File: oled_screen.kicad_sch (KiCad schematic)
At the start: 7 parts, among them U38 0.96 OLED Display 8 pins

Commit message: SBCv0.3
there is no big thing update just some LCSC & Mouser parts
and Big problem deleted alot of component values (:
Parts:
- removed C397: 10u, Capacitor_SMD:C_0201_0603Metric_Pad0.64x0.40mm_HandSolder, symbol New_Library_0:C_Small_edited
- added C112: 10u, Capacitor_SMD:C_0603_1608Metric, symbol New_Library_0:C_Small_edited
- C394: LCSC Part (none) -> C19702; Mouser Part (none) -> 187-CL10A106KP8NNNC
- C395, C396: LCSC Part (none) -> C5209398; Mouser Part (none) -> CL03A105KP3NSNC
- R188: value 10k -> (none); LCSC Part (none) -> (at 0 0 0)
- R189: value 100R -> (none); LCSC Part (none) -> (polyline
- U38: value 0.96 OLED Display 8 pins -> (none); LCSC Part C5139767 -> (none); Mouser Part (none) -> )
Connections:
- net GND: now also C112.2
- net OLED_LED: now also C112.1

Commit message: SBCv0.4
add LCSC & Mouser parts 
and solve the deleted value in the past version
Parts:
- removed R188: (no value), PCM_Resistor_SMD_AKL:R_0402_1005Metric, symbol Device:R_Small
- removed U38: (no value), Datasheet_Footprints:FFC-SMD_8P-P0.50_AFC42-S08FMA-1H_BOTTOM, symbol Datasheet_Symbols:OLED Dosplay 8 pins
- added R246: 240R, PCM_Resistor_SMD_AKL:R_0402_1005Metric, symbol Device:R_Small
- added U53: 0.96 OLED Display 8 pins, Datasheet_Footprints:FFC-SMD_8P-P0.50_AFC42-S08FMA-1H_BOTTOM, symbol Datasheet_Symbols:OLED Dosplay 8 pins
- R189: value (none) -> 10k; footprint PCM_Resistor_SMD_AKL:R_0402_1005Metric_Pad0.72x0.64mm -> PCM_Resistor_SMD_AKL:R_0402_1005Metric; LCSC Part (polyline -> C60490; Mouser Part (none) -> 603-RC0402FR-0710KL
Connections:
- net GND: now also U53.2 (GND)
- net OLED_CLK: now also U53.6 (SCL)
- net OLED_CS: now also U53.8 (CS)
- net OLED_LED: now also R246.2, U53.1 (LEDA); no longer R189.2
- net OLED_MOSI: now also U53.5 (SDA)
- net OLED_RESET: now also R189.2, U53.3 (RESET)
- net OLED_RS: now also U53.4 (RS)
- net VCC5V0_SYS: now also R246.1; no longer R189.1
- net VCC_3V3_S0: now also R189.1, U53.7 (VDD)

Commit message: Release v2: replace main with RK3576 SBCv2, archive v1 to branch archive/v1
- main now shows only v2 (RK3576 SBCv2.kicad_pro)
- v1 preserved in branch archive/v1 + tag v1.0
- Add .gitignore for KiCad (*.bak, *.lck, .history/)
- Update README with version switcher
- Cleaned: dropped 141M .history, Resources ref PDF, *.bak/*.lck
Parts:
- removed R189: 10k, PCM_Resistor_SMD_AKL:R_0402_1005Metric, symbol Device:R_Small
- removed R246: 240R, PCM_Resistor_SMD_AKL:R_0402_1005Metric, symbol Device:R_Small
- added R197: 10k, PCM_Resistor_SMD_AKL:R_0402_1005Metric, symbol Device:R_Small
- added R251: 240R, PCM_Resistor_SMD_AKL:R_0402_1005Metric, symbol Device:R_Small
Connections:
- net OLED_LED: now also R251.2
- net OLED_RESET: now also R197.2
- net VCC5V0_SYS: now also R251.1
- net VCC_3V3_S0: now also R197.1

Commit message: Relink hierarchical root: 18 sheets into RK3576 SBCv2 top level
Root was empty (no sheet boxes); all subsheets orphaned.
Rebuilt A1 top level linking RK3576, LPDDR5, Power, Ethernet,
HDMI, MIPI, PCIe, USB-A/C, Wireless, RTC, uSD, GPIO, OLED,
RP2350A, Connectors, Fixtures, DC_Power. block_diagrame kept
docs-only (unlinked, avoids double-instantiation). Lowercase
stub duplicates excluded. ERC: 1388 -> 770 violations.
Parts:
- removed U53: 0.96 OLED Display 8 pins, Datasheet_Footprints:FFC-SMD_8P-P0.50_AFC42-S08FMA-1H_BOTTOM, symbol Datasheet_Symbols:OLED Dosplay 8 pins
- added U45: 0.96 OLED Display 8 pins, Datasheet_Footprints:FFC-SMD_8P-P0.50_AFC42-S08FMA-1H_BOTTOM, symbol Datasheet_Symbols:OLED Dosplay 8 pins
- renumbered C394 to C343, C395 to C344, C396 to C345, C112 to C346, R251 to R205, R197 to R206
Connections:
- net GND: now also U45.2 (GND)
- net OLED_CLK: now also U45.6 (SCL)
- net OLED_CS: now also U45.8 (CS)
- net OLED_LED: now also U45.1 (LEDA)
- net OLED_MOSI: now also U45.5 (SDA)
- net OLED_RESET: now also U45.3 (RESET)
- net OLED_RS: now also U45.4 (RS)
- net VCC_3V3_S0: now also U45.7 (VDD)
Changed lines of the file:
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@@
 		(in_pos_files yes)
 		(dnp no)
-		(property "Reference" "#PWR0573"
+		(property "Reference" "#PWR0520"
 			(at 96.52 92.71 0)
 			(hide yes)
@@
 			(project "RK3576 SBCv2"
 				(path "/802f5b9f-44c6-4b1a-a63a-2c094d5816db/07d8ed82-8848-42fe-9400-02853b4a0afe"
-					(reference "#PWR0573")
+					(reference "#PWR0520")
 					(unit 1)
 				)
@@
 		(in_pos_files yes)
 		(dnp no)
-		(property "Reference" "#PWR0570"
+		(property "Reference" "#PWR0517"
 			(at 53.34 80.01 0)
 			(hide yes)
@@
 			(project "RK3576 SBCv2"
 				(path "/802f5b9f-44c6-4b1a-a63a-2c094d5816db/07d8ed82-8848-42fe-9400-02853b4a0afe"
-					(reference "#PWR0570")
+					(reference "#PWR0517")
 					(unit 1)
 				)
@@
 		(dnp no)
 		(fields_autoplaced yes)
-		(property "Reference" "C394"
+		(property "Reference" "C343"
 			(at 55.88 49.5362 0)
 			(show_name no)
@@
 			(project "RK3576 SBCv2"
 				(path "/802f5b9f-44c6-4b1a-a63a-2c094d5816db/07d8ed82-8848-42fe-9400-02853b4a0afe"
-					(reference "C394")
+					(reference "C343")
 					(unit 1)
 				)
@@
 		(in_pos_files yes)
 		(dnp no)
-		(property "Reference" "#PWR0572"
+		(property "Reference" "#PWR0519"
 			(at 85.09 92.71 0)
 			(hide yes)
@@
 			(project "RK3576 SBCv2"
 				(path "/802f5b9f-44c6-4b1a-a63a-2c094d5816db/07d8ed82-8848-42fe-9400-02853b4a0afe"
-					(reference "#PWR0572")
+					(reference "#PWR0519")
 					(unit 1)
 				)
@@
 		(in_pos_files yes)
 		(dnp no)
-		(property "Reference" "#PWR0568"
+		(property "Reference" "#PWR0515"
 			(at 53.34 49.53 0)
 			(hide yes)
@@
 			(project "RK3576 SBCv2"
 				(path "/802f5b9f-44c6-4b1a-a63a-2c094d5816db/07d8ed82-8848-42fe-9400-02853b4a0afe"
-					(reference "#PWR0568")
+					(reference "#PWR0515")
 					(unit 1)
 				)
@@
 		(in_pos_files yes)
 		(dnp no)
-		(property "Reference" "R251"
+		(property "Reference" "R205"
 			(at 59.69 80.01 90)
 			(show_name no)
@@
 			(project "RK3576 SBCv2"
 				(path "/802f5b9f-44c6-4b1a-a63a-2c094d5816db/07d8ed82-8848-42fe-9400-02853b4a0afe"
-					(reference "R251")
+					(reference "R205")
 					(unit 1)
 				)
@@
 		(in_pos_files yes)
 		(dnp no)
-		(property "Reference" "R197"
+		(property "Reference" "R206"
 			(at 85.344 49.53 0)
 			(show_name no)
@@
 			(project "RK3576 SBCv2"
 				(path "/802f5b9f-44c6-4b1a-a63a-2c094d5816db/07d8ed82-8848-42fe-9400-02853b4a0afe"
-					(reference "R197")
+					(reference "R206")
 					(unit 1)
 				)
@@
 		(in_pos_files yes)
 		(dnp no)
-		(property "Reference" "C396"
+		(property "Reference" "C345"
 			(at 71.12 82.5562 0)
 			(show_name no)
@@
 			(project "RK3576 SBCv2"
 				(path "/802f5b9f-44c6-4b1a-a63a-2c094d5816db/07d8ed82-8848-42fe-9400-02853b4a0afe"
-					(reference "C396")
+					(reference "C345")
 					(unit 1)
 				)
@@
 		(in_pos_files yes)
 		(dnp no)
-		(property "Reference" "#PWR0569"
+		(property "Reference" "#PWR0516"
 			(at 53.34 60.96 0)
 			(hide yes)
@@
 			(project "RK3576 SBCv2"
 				(path "/802f5b9f-44c6-4b1a-a63a-2c094d5816db/07d8ed82-8848-42fe-9400-02853b4a0afe"
-					(reference "#PWR0569")
+					(reference "#PWR0516")
 					(unit 1)
 				)
@@
 		(in_pos_files yes)
 		(dnp no)
-		(property "Reference" "#PWR0571"
+		(property "Reference" "#PWR0518"
 			(at 73.66 92.71 0)
 			(hide yes)
@@
 			(project "RK3576 SBCv2"
 				(path "/802f5b9f-44c6-4b1a-a63a-2c094d5816db/07d8ed82-8848-42fe-9400-02853b4a0afe"
-					(reference "#PWR0571")
+					(reference "#PWR0518")
 					(unit 1)
 				)
@@
 		(dnp no)
 		(fields_autoplaced yes)
-		(property "Reference" "C112"
+		(property "Reference" "C346"
 			(at 87.63 82.5562 0)
 			(show_name no)
@@
 			(project "RK3576 SBCv2"
 				(path "/802f5b9f-44c6-4b1a-a63a-2c094d5816db/07d8ed82-8848-42fe-9400-02853b4a0afe"
-					(reference "C112")
+					(reference "C346")
 					(unit 1)
 				)
@@
 		(dnp no)
 		(fields_autoplaced yes)
-		(property "Reference" "U53"
+		(property "Reference" "U45"
 			(at 142.24 72.3899 0)
 			(show_name no)
@@
 			(project "RK3576 SBCv2"
 				(path "/802f5b9f-44c6-4b1a-a63a-2c094d5816db/07d8ed82-8848-42fe-9400-02853b4a0afe"
-					(reference "U53")
+					(reference "U45")
 					(unit 1)
 				)
@@
 		(in_pos_files yes)
 		(dnp no)
-		(property "Reference" "C395"
+		(property "Reference" "C344"
 			(at 64.77 49.5362 0)
 			(show_name no)
@@
 			(project "RK3576 SBCv2"
 				(path "/802f5b9f-44c6-4b1a-a63a-2c094d5816db/07d8ed82-8848-42fe-9400-02853b4a0afe"
-					(reference "C395")
+					(reference "C344")
 					(unit 1)
 				)

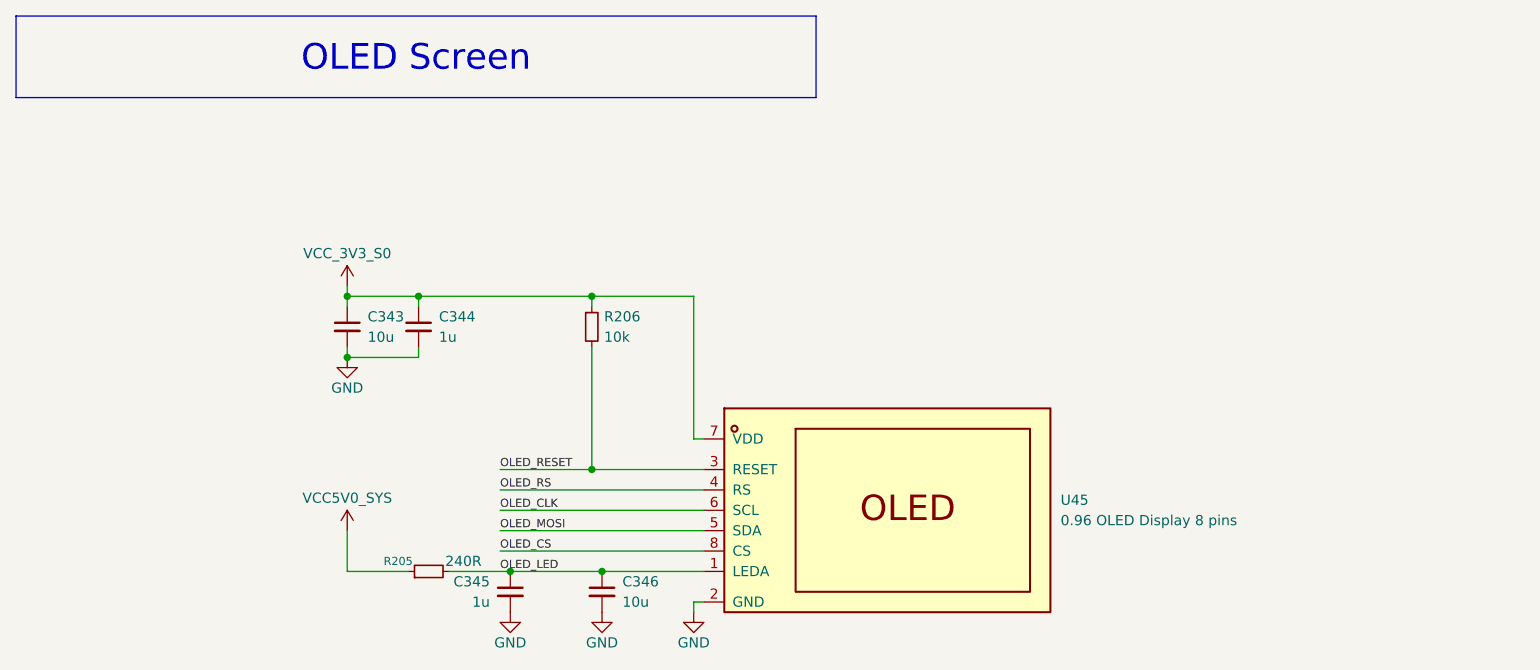
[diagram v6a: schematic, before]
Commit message: Update v2 schematics + PCB: impedance profiles, design rules, sheet fixes
- pro: copper/track widths, microvias, 40/50 OHM + DIFF 85/90/100 tuning profiles
- dru/pcb: updated constraints and layout
- sheets: RK3576, RP2350A, Fixtures, MIPI, PCIe, HDMI, LPDDR5, UFS/eMMC, OLED, block diagram
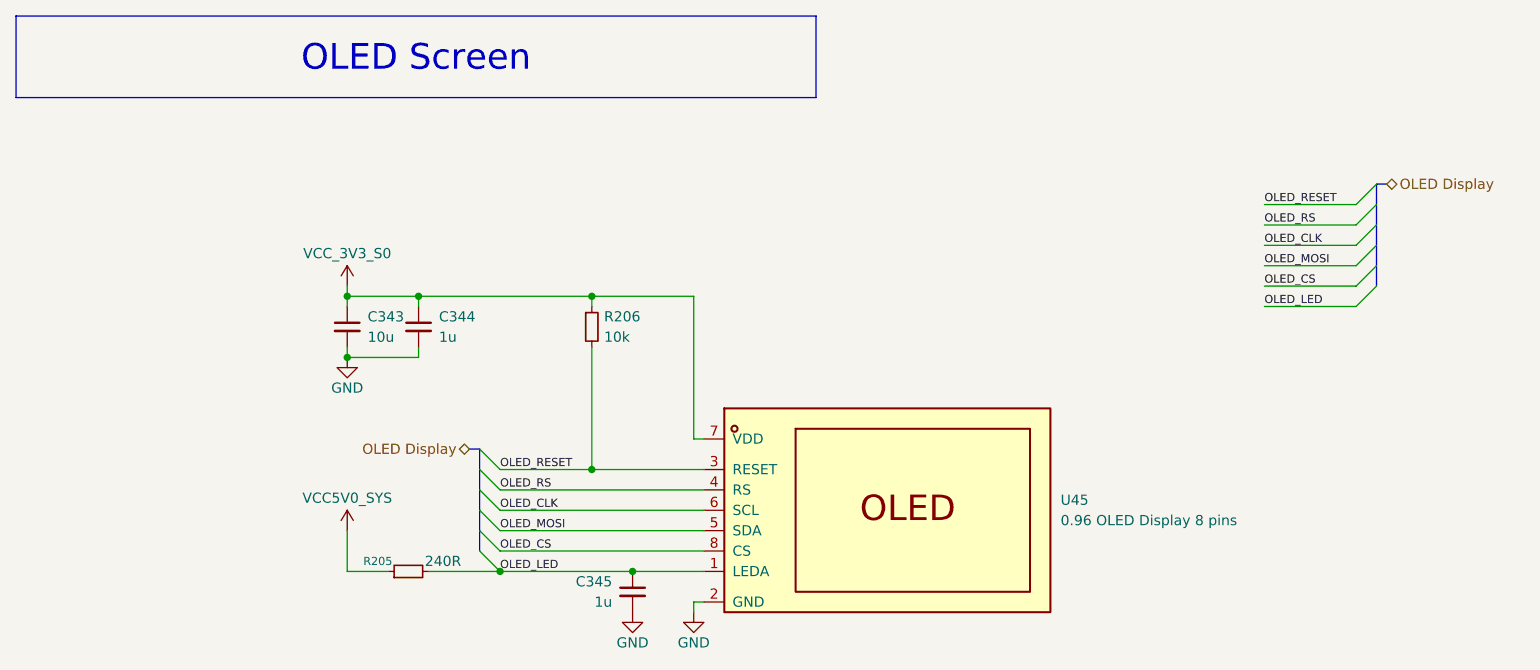
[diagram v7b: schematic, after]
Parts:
- removed C346: 10u, Capacitor_SMD:C_0603_1608Metric, symbol New_Library_0:C_Small_edited
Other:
- moved on the sheet: C345, R205

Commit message: block diagrame with Hierarchical labels and NVMe SSD footprint
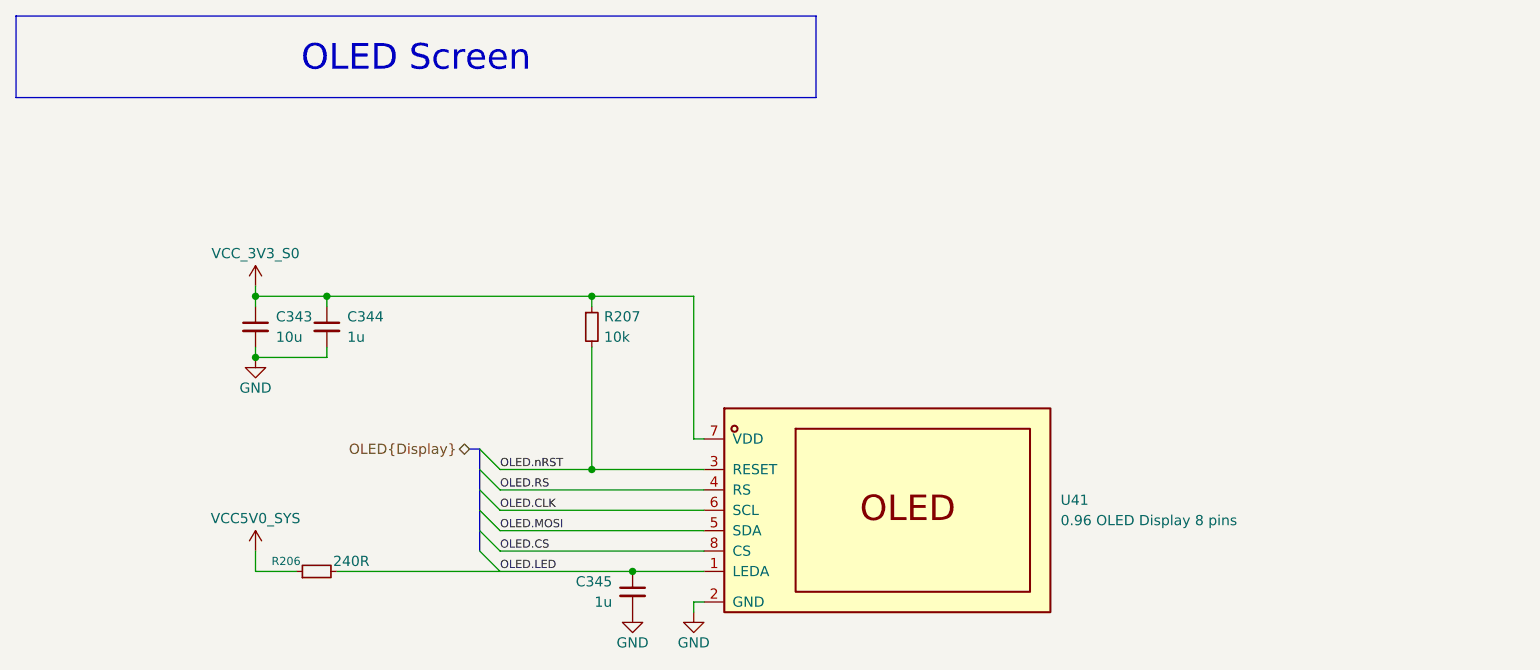
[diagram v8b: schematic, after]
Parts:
- renumbered R205 to R206, R206 to R207, U45 to U41
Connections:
- net OLED_CLK renamed OLED.CLK
- net OLED_CS renamed OLED.CS
- net OLED_LED renamed OLED.LED
- net OLED_MOSI renamed OLED.MOSI
- net OLED_RESET renamed OLED.nRST
- net OLED_RS renamed OLED.RS
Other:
- moved on the sheet: C343, C344, R206
